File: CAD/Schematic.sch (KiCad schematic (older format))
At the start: 8 parts, among them U1 4N35

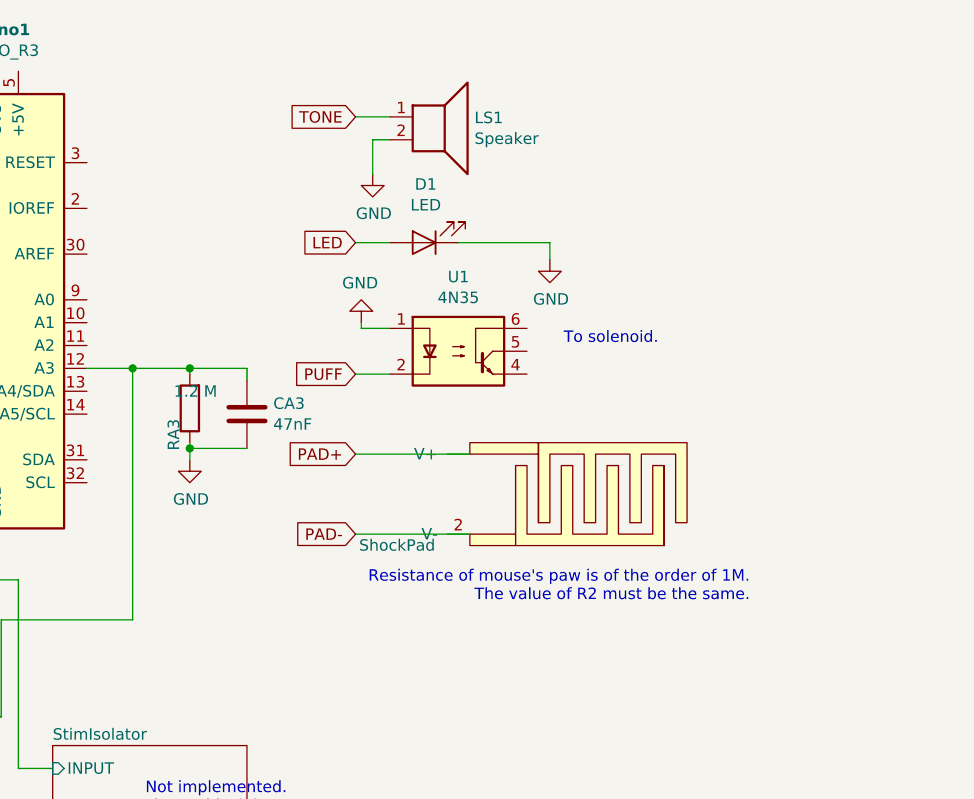
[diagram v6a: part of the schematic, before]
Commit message: Fixed the nasty bug. Updated CAD designs.
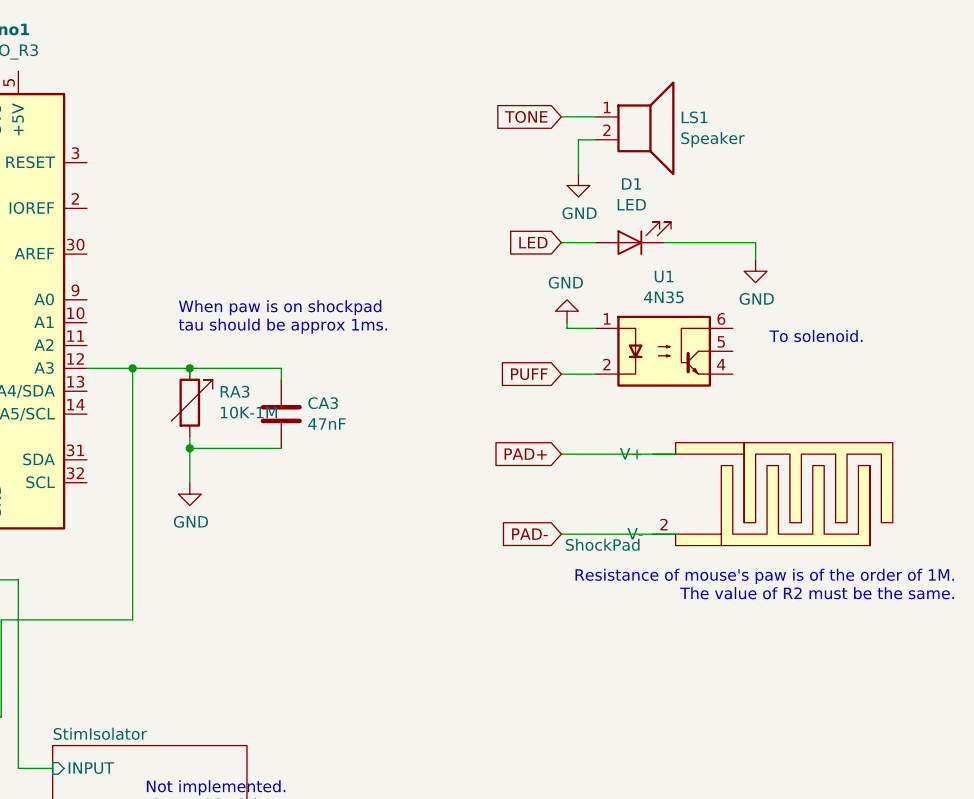
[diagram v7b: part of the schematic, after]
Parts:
- removed RA3: 1.2 M, symbol Device:R
- added RA3: 10K-1M, symbol Device:R_Variable
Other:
- note added: "When paw is on shockpad\ntau should be approx 1ms."
- moved on the sheet: CA3, D1, LS1, U1
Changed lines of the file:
@@
 L Device:Speaker LS1
 U 1 1 5D18ABCB
-P 6925 2150
-F 0 "LS1" H 7095 2146 50  0000 L CNN
-F 1 "Speaker" H 7095 2055 50  0000 L CNN
-F 2 "" H 6925 1950 50  0001 C CNN
-F 3 "~" H 6915 2100 50  0001 C CNN
-	1    6925 2150
-	1    0    0    -1
-$EndComp
-$Comp
-L Device:LED D1
-U 1 1 5D18B2CE
-P 6875 2700
-F 0 "D1" H 6868 2445 50  0000 C CNN
-F 1 "LED" H 6868 2536 50  0000 C CNN
-F 2 "" H 6875 2700 50  0001 C CNN
-F 3 "~" H 6875 2700 50  0001 C CNN
-	1    6875 2700
-	-1   0    0    1
-$EndComp
-$Comp
-L Isolator:4N35 U1
-U 1 1 5D188B23
-P 7025 3175
-F 0 "U1" H 7025 3500 50  0000 C CNN
-F 1 "4N35" H 7025 3409 50  0000 C CNN
-F 2 "Package_DIP:DIP-6_W7.62mm" H 6825 2975 50  0001 L CIN
-F 3 "https://www.vishay.com/docs/81181/4n35.pdf" H 7025 3175 50  0001 L CNN
-	1    7025 3175
-	1    0    0    -1
-$EndComp
-$Comp
-L power:GND #PWR0101
-U 1 1 5D189E2E
-P 6600 3050
-F 0 "#PWR0101" H 6600 2800 50  0001 C CNN
-F 1 "GND" H 6605 2877 50  0000 C CNN
-F 2 "" H 6600 3050 50  0001 C CNN
-F 3 "" H 6600 3050 50  0001 C CNN
-	1    6600 3050
-	-1   0    0    1
-$EndComp
-Wire Wire Line
-	6725 3075 6600 3075
-Wire Wire Line
-	6600 3075 6600 3050
+P 7825 2150
+F 0 "LS1" H 7995 2146 50  0000 L CNN
+F 1 "Speaker" H 7995 2055 50  0000 L CNN
+F 2 "" H 7825 1950 50  0001 C CNN
+F 3 "~" H 7815 2100 50  0001 C CNN
+	1    7825 2150
+	1    0    0    -1
+$EndComp
 Text GLabel 4075 3150 0    50   Input ~ 0
 TONE
@@
 Wire Wire Line
 	4075 3650 4400 3650
-Text GLabel 6575 2150 0    50   Input ~ 0
+Text GLabel 7475 2150 0    50   Input ~ 0
 TONE
 Wire Wire Line
-	6575 2150 6725 2150
-Text GLabel 6575 2700 0    50   Input ~ 0
-LED
-Wire Wire Line
-	6575 2700 6725 2700
-Text GLabel 6575 3275 0    50   Input ~ 0
-PUFF
-Wire Wire Line
-	6575 3275 6725 3275
-$Comp
-L power:GND #PWR0102
-U 1 1 5D18C223
-P 7425 2775
-F 0 "#PWR0102" H 7425 2525 50  0001 C CNN
-F 1 "GND" H 7430 2602 50  0000 C CNN
-F 2 "" H 7425 2775 50  0001 C CNN
-F 3 "" H 7425 2775 50  0001 C CNN
-	1    7425 2775
-	1    0    0    -1
-$EndComp
-Wire Wire Line
-	7025 2700 7425 2700
-Wire Wire Line
-	7425 2700 7425 2775
+	7475 2150 7625 2150
 $Comp
 L power:GND #PWR0103
 U 1 1 5D18CB7D
-P 6650 2400
-F 0 "#PWR0103" H 6650 2150 50  0001 C CNN
-F 1 "GND" H 6655 2227 50  0000 C CNN
-F 2 "" H 6650 2400 50  0001 C CNN
-F 3 "" H 6650 2400 50  0001 C CNN
-	1    6650 2400
-	1    0    0    -1
-$EndComp
-Wire Wire Line
-	6725 2250 6650 2250
-Wire Wire Line
-	6650 2250 6650 2400
-Text Notes 7900 3150 2    50   ~ 0
-To solenoid.
+P 7550 2400
+F 0 "#PWR0103" H 7550 2150 50  0001 C CNN
+F 1 "GND" H 7555 2227 50  0000 C CNN
+F 2 "" H 7550 2400 50  0001 C CNN
+F 3 "" H 7550 2400 50  0001 C CNN
+	1    7550 2400
+	1    0    0    -1
+$EndComp
+Wire Wire Line
+	7625 2250 7550 2250
+Wire Wire Line
+	7550 2250 7550 2400
 Text Notes 2350 2175 0    50   ~ 0
 1200 counts per cycle.
@@
 Wire Wire Line
 	5600 3250 5400 3250
-$Comp
-L Schematic-rescue:ShockPad-BhallaLabComponents-Schematic-rescue ShockPad1
-U 1 1 5D197A8E
-P 7525 3775
-F 0 "ShockPad1" H 7875 3625 50  0001 C CNN
-F 1 "ShockPad" H 6757 3555 50  0000 C TNN
-F 2 "" H 7875 3625 50  0001 C CNN
-F 3 "" H 7875 3625 50  0001 C CNN
-	1    7525 3775
-	1    0    0    -1
-$EndComp
-Text GLabel 6575 3625 0    50   Input ~ 0
-PAD+
-Text GLabel 6575 3975 0    50   Input ~ 0
-PAD-
-Wire Wire Line
-	6575 3625 7075 3625
-Wire Wire Line
-	6575 3975 7075 3975
 Wire Wire Line
 	4175 4175 5100 4175
 Wire Wire Line
 	5600 4350 5600 3250
-$Comp
-L Device:R RA3
-U 1 1 5D1B22CC
-P 5850 3425
-F 0 "RA3" V 5920 3471 50  0000 L CNN
-F 1 "1.2 M" H 5920 3380 50  0000 R TNN
-F 2 "" V 5780 3425 50  0001 C CNN
-F 3 "~" H 5850 3425 50  0001 C CNN
-	1    5850 3425
-	-1   0    0    1
-$EndComp
 $Comp
 L power:GND #PWR0106
 U 1 1 5D1B2935
-P 5850 3650
-F 0 "#PWR0106" H 5850 3400 50  0001 C CNN
-F 1 "GND" H 5855 3477 50  0000 C CNN
-F 2 "" H 5850 3650 50  0001 C CNN
-F 3 "" H 5850 3650 50  0001 C CNN
-	1    5850 3650
-	1    0    0    -1
-$EndComp
-Wire Wire Line
-	5850 3575 5850 3600
+P 5850 3750
+F 0 "#PWR0106" H 5850 3500 50  0001 C CNN
+F 1 "GND" H 5855 3577 50  0000 C CNN
+F 2 "" H 5850 3750 50  0001 C CNN
+F 3 "" H 5850 3750 50  0001 C CNN
+	1    5850 3750
+	1    0    0    -1
+$EndComp
 Wire Wire Line
 	5850 3275 5850 3250
@@
 Text Notes 6275 5200 2    50   ~ 0
 Not implemented.\nUsing as black-box.
-Text Notes 8300 4275 2    50   ~ 0
+Text Notes 9200 4275 2    50   ~ 0
 Resistance of mouse's paw is of the order of 1M.\nThe value of R2 must be the same.
 $Comp
@@
 Wire Wire Line
 	3200 4700 3200 4650
-$Comp
-L Device:C CA3
-U 1 1 5D1B6EF2
-P 6100 3450
-F 0 "CA3" H 6215 3496 50  0000 L CNN
-F 1 "47nF" H 6215 3405 50  0000 L CNN
-F 2 "" H 6138 3300 50  0001 C CNN
-F 3 "~" H 6100 3450 50  0001 C CNN
-	1    6100 3450
-	1    0    0    -1
-$EndComp
-Wire Wire Line
-	6100 3300 6100 3250
-Wire Wire Line
-	6100 3250 5850 3250
 Connection ~ 5850 3250
-Wire Wire Line
-	6100 3600 5850 3600
-Connection ~ 5850 3600
-Wire Wire Line
-	5850 3600 5850 3650
 $Sheet
 S 3400 4500 1125 950
@@
 Text Notes 3600 5000 0    50   ~ 0
 Low Level Trigger.\nVendor: NA \nAsk hrishi@ncbs.res.in
+$Comp
+L Device:R_Variable RA3
+U 1 1 5D1DDD1C
+P 5850 3400
+F 0 "RA3" H 5978 3446 50  0000 L CNN
+F 1 "10K-1M" H 5978 3355 50  0000 L CNN
+F 2 "" V 5780 3400 50  0001 C CNN
+F 3 "~" H 5850 3400 50  0001 C CNN
+	1    5850 3400
+	1    0    0    -1
+$EndComp
+$Comp
+L Device:C CA3
+U 1 1 5D1B6EF2
+P 6250 3450
+F 0 "CA3" H 6365 3496 50  0000 L CNN
+F 1 "47nF" H 6365 3405 50  0000 L CNN
+F 2 "" H 6288 3300 50  0001 C CNN
+F 3 "~" H 6250 3450 50  0001 C CNN
+	1    6250 3450
+	1    0    0    -1
+$EndComp
+Wire Wire Line
+	5850 3600 5850 3750
+Wire Wire Line
+	5850 3550 5850 3600
+Connection ~ 5850 3600
+Wire Wire Line
+	5850 3600 6250 3600
+Wire Wire Line
+	6250 3300 6250 3250
+Wire Wire Line
+	5850 3250 6250 3250
+Wire Wire Line
+	7475 3975 7975 3975
+Wire Wire Line
+	7475 3625 7975 3625
+Text GLabel 7475 3975 0    50   Input ~ 0
+PAD-
+Text GLabel 7475 3625 0    50   Input ~ 0
+PAD+
+$Comp
+L Schematic-rescue:ShockPad-BhallaLabComponents-Schematic-rescue ShockPad1
+U 1 1 5D197A8E
+P 8425 3775
+F 0 "ShockPad1" H 8775 3625 50  0001 C CNN
+F 1 "ShockPad" H 7657 3555 50  0000 C TNN
+F 2 "" H 8775 3625 50  0001 C CNN
+F 3 "" H 8775 3625 50  0001 C CNN
+	1    8425 3775
+	1    0    0    -1
+$EndComp
+Text Notes 8800 3150 2    50   ~ 0
+To solenoid.
+Wire Wire Line
+	8325 2700 8325 2775
+Wire Wire Line
+	7925 2700 8325 2700
+$Comp
+L power:GND #PWR0102
+U 1 1 5D18C223
+P 8325 2775
+F 0 "#PWR0102" H 8325 2525 50  0001 C CNN
+F 1 "GND" H 8330 2602 50  0000 C CNN
+F 2 "" H 8325 2775 50  0001 C CNN
+F 3 "" H 8325 2775 50  0001 C CNN
+	1    8325 2775
+	1    0    0    -1
+$EndComp
+Wire Wire Line
+	7475 3275 7625 3275
+Text GLabel 7475 3275 0    50   Input ~ 0
+PUFF
+Wire Wire Line
+	7475 2700 7625 2700
+Text GLabel 7475 2700 0    50   Input ~ 0
+LED
+Wire Wire Line
+	7500 3075 7500 3050
+Wire Wire Line
+	7625 3075 7500 3075
+$Comp
+L power:GND #PWR0101
+U 1 1 5D189E2E
+P 7500 3050
+F 0 "#PWR0101" H 7500 2800 50  0001 C CNN
+F 1 "GND" H 7505 2877 50  0000 C CNN
+F 2 "" H 7500 3050 50  0001 C CNN
+F 3 "" H 7500 3050 50  0001 C CNN
+	1    7500 3050
+	-1   0    0    1
+$EndComp
+$Comp
+L Isolator:4N35 U1
+U 1 1 5D188B23
+P 7925 3175
+F 0 "U1" H 7925 3500 50  0000 C CNN
+F 1 "4N35" H 7925 3409 50  0000 C CNN
+F 2 "Package_DIP:DIP-6_W7.62mm" H 7725 2975 50  0001 L CIN
+F 3 "https://www.vishay.com/docs/81181/4n35.pdf" H 7925 3175 50  0001 L CNN
+	1    7925 3175
+	1    0    0    -1
+$EndComp
+$Comp
+L Device:LED D1
+U 1 1 5D18B2CE
+P 7775 2700
+F 0 "D1" H 7768 2445 50  0000 C CNN
+F 1 "LED" H 7768 2536 50  0000 C CNN
+F 2 "" H 7775 2700 50  0001 C CNN
+F 3 "~" H 7775 2700 50  0001 C CNN
+	1    7775 2700
+	-1   0    0    1
+$EndComp
+Text Notes 5800 3100 0    50   ~ 0
+When paw is on shockpad\ntau should be approx 1ms.
 $EndSCHEMATC
